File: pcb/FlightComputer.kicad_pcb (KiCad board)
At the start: 2 copper layers, 23 x 50.2 mm, 74 parts, among them J1 USB4105-GF-A, Q1 DMG3415U, Q2 Si2319CDS, Q3 Si2319CDS, SW1 RESET, SW2 BOOT, U2 ICM-42670-P, U3 ESP32-C3-MINI-1, U5 SY8088, U6 MCP73831T-2ACI/OT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

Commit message: change Si2319CDS to Si2302CDS
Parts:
- Q2, Q3: value Si2319CDS -> Si2302CDS
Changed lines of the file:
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@@
 			)
 		)
-		(property "Value" "Si2319CDS"
+		(property "Value" "Si2302CDS"
 			(at 0 2.4 90)
 			(layer "F.Fab")
@@
 			)
 		)
-		(property "LCSC" "C146287"
+		(property "LCSC" "C10488"
 			(at 0 0 -90)
 			(unlocked yes)
@@
 			)
 		)
-		(property "Value" "Si2319CDS"
+		(property "Value" "Si2302CDS"
 			(at 0 2.4 90)
 			(layer "F.Fab")
@@
 			)
 		)
-		(property "Datasheet" "http://www.vishay.com/docs/66709/si2319cd.pdf"
+		(property "Datasheet" ""
 			(at 0 0 -90)
 			(unlocked yes)
@@
 			)
 		)
-		(property "Description" "-4.4A Id, -40V Vds, P-Channel MOSFET, SOT-23"
+		(property "Description" "N-MOSFET transistor, gate/source/drain"
 			(at 0 0 -90)
 			(unlocked yes)
@@
 			)
 		)
-		(property "LCSC" "C146287"
+		(property "LCSC" "C10488"
 			(at 0 0 -90)
 			(unlocked yes)
@@
 			)
 		)
-		(property ki_fp_filters "SOT?23*")
 		(sheetname "Root")
 		(sheetfile "FlightComputer.kicad_sch")

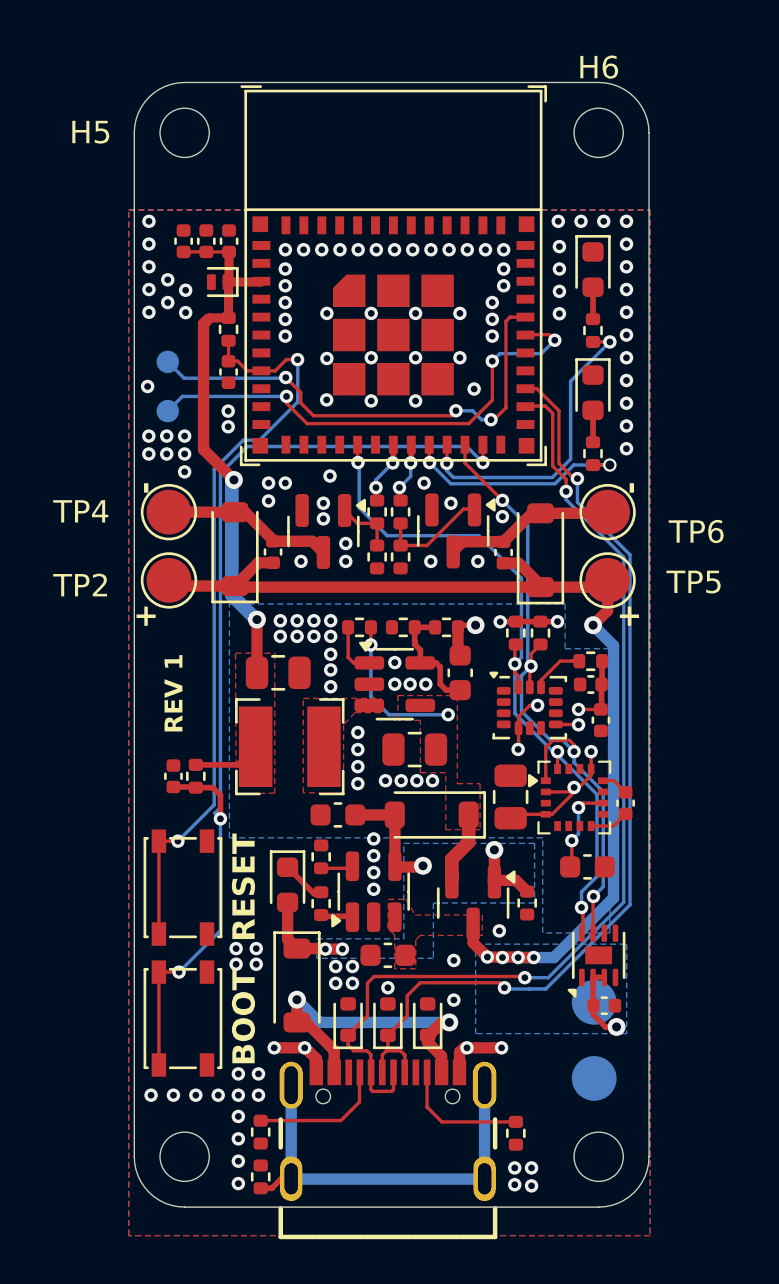
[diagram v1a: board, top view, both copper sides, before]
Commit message: Move battery pads to front
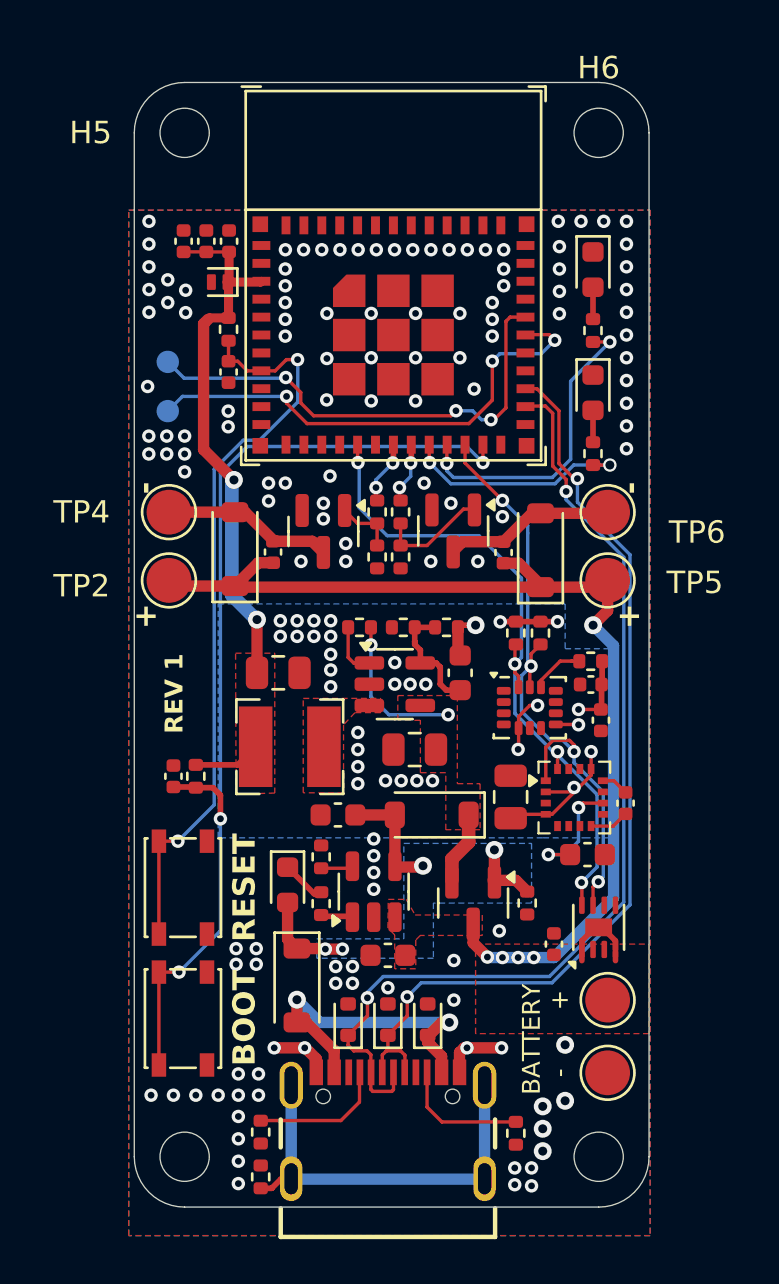
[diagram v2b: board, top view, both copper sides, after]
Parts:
- H1, H2: moved to F.Cu
- moved C18 3.55 mm to (155.5, 115.5), turned to 90 degrees
- moved U7 1.25 mm to (157.5, 114.8)
- moved H2 0.65 mm to (157.9, 121.2), turned to 0 degrees
- moved H1 0.61 mm to (157.9, 118.0), turned to 0 degrees
- moved C19 0.55 mm to (157.0, 111.5)
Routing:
- net +BATT: track 50.8 -> 46.7 mm, vias 6 -> 5
- net GND: track 5.54 -> 9.09 mm, vias 145 -> 150
- net IO10_SDA: track 32.2 -> 30.9 mm
- net Net-(U9-CAP): track 3.98 -> 5.24 mm
- net IO8_SCL: track 30.6 -> 29.4 mm
- removed copper zone on B.Cu, net +BATT
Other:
- board text added: "BATTERY"
- board text removed: "B+"
- board text removed: "B-"
